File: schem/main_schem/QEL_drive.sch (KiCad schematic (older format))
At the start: 7 parts

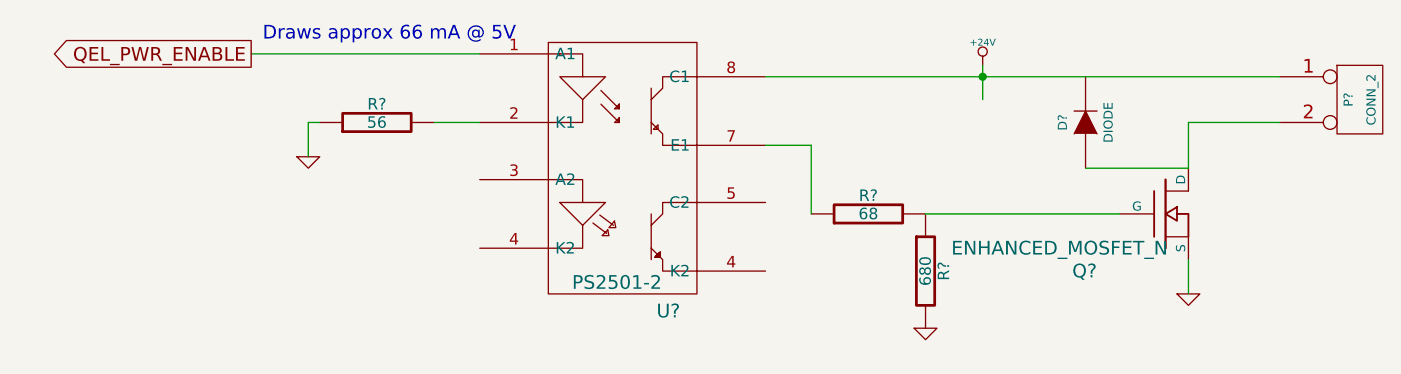
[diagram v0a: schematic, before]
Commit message: Vdd and ethernet conns to mcu
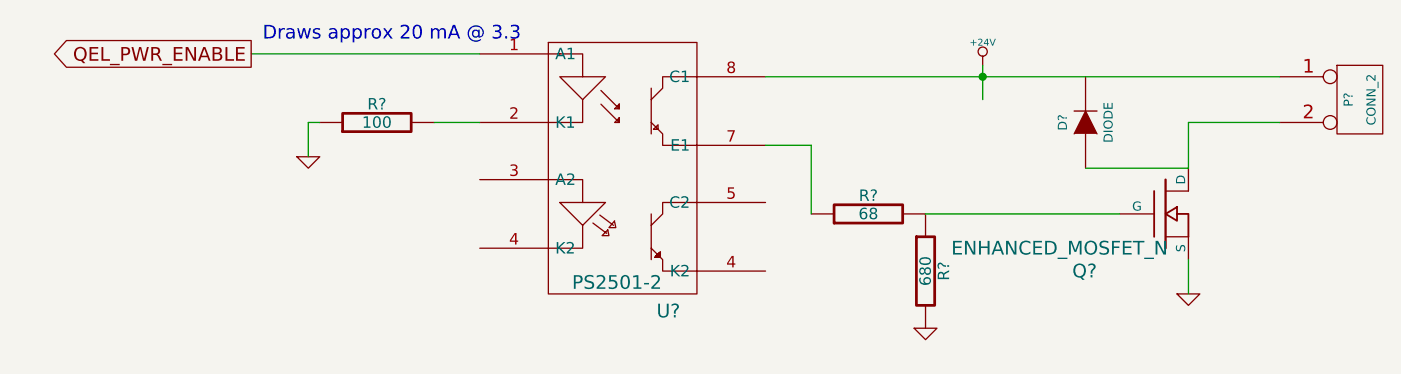
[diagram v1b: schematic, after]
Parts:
- R?: value 56 -> 100
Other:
- note added: "Draws approx 20 mA @ 3.3"
- note removed: "Draws approx 66 mA @ 5V"
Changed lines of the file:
@@
-EESchema Schematic File Version 2  date 9/18/2012 3:41:36 PM
+EESchema Schematic File Version 2  date 9/28/2012 9:39:08 AM
 LIBS:power
 LIBS:device
@@
 LIBS:valves
 LIBS:QEL
+LIBS:pic18f97j60
+LIBS:pwr
 LIBS:main_schem-cache
 EELAYER 25  0
@@
 Sheet 2 6
 Title "QEL_Driver"
-Date "18 sep 2012"
+Date "28 sep 2012"
 Rev "2"
 Comp "ECE 402 Senior Design"
@@
 $EndComp
 Text Notes 4100 3300 0    60   ~ 0
-Draws approx 66 mA @ 5V
+Draws approx 20 mA @ 3.3
 $Comp
 L R R?
@@
 P 4600 3650
 F 0 "R?" V 4680 3650 50  0000 C CNN
-F 1 "56" V 4600 3650 50  0000 C CNN
+F 1 "100" V 4600 3650 50  0000 C CNN
 	1    4600 3650
 	0    -1   -1   0

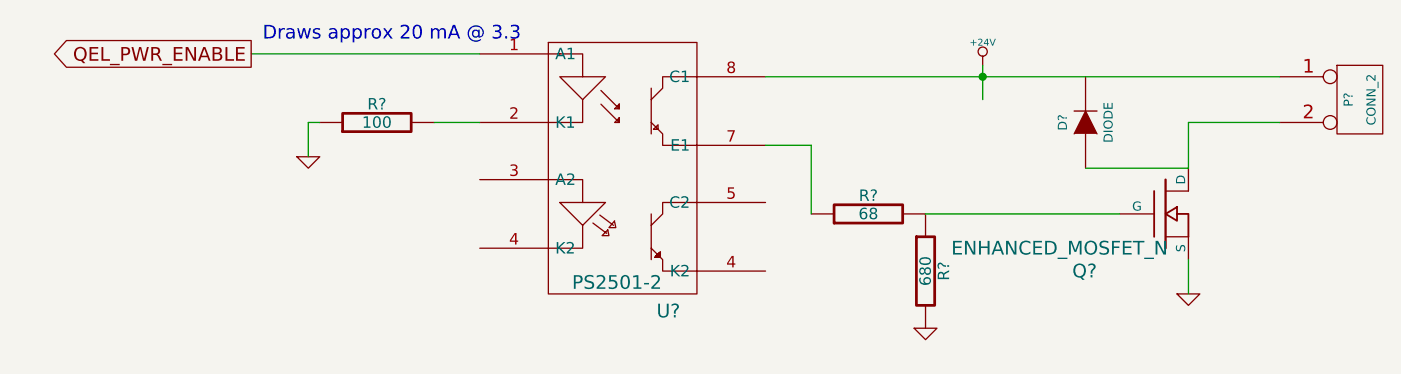
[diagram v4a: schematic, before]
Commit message: linear regulators for logic/mcu
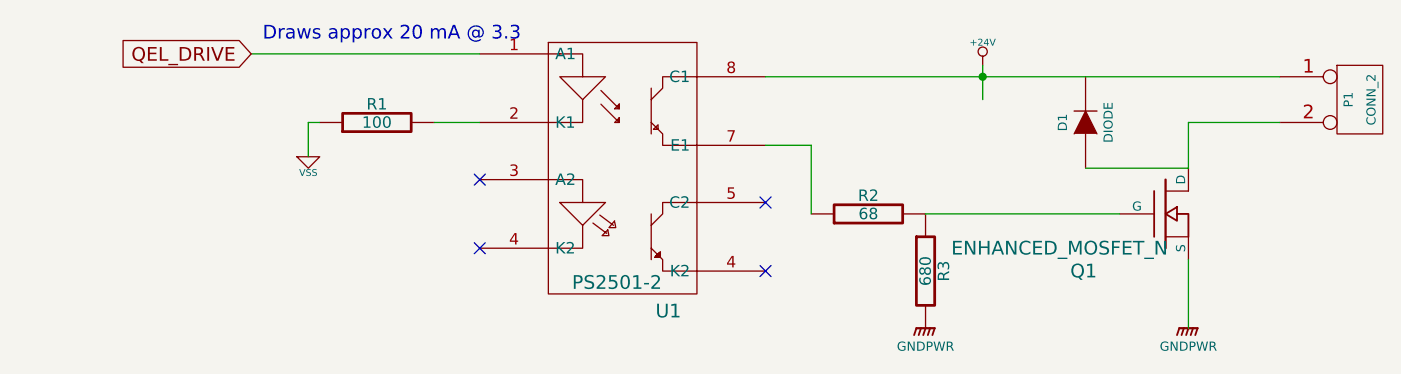
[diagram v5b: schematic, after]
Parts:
- gave numbers to parts that had none: 7
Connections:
- net labels added: GNDPWR, QEL_DRIVE, VSS
- net labels removed: GND, QEL_PWR_ENABLE
- no-connect marks 0 -> 4
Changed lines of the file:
@@
-EESchema Schematic File Version 2  date 9/29/2012 1:33:09 PM
+EESchema Schematic File Version 2  date 9/29/2012 2:30:36 PM
 LIBS:power
 LIBS:device
@@
 Comment4 ""
 $EndDescr
+Wire Wire Line
+	8150 4550 8150 4250
+Wire Wire Line
+	7000 4050 7850 4050
+Wire Wire Line
+	8150 3650 8150 3850
+Wire Wire Line
+	8550 3450 6300 3450
+Wire Wire Line
+	7250 3550 7250 3400
+Wire Wire Line
+	4850 3650 5050 3650
+Wire Wire Line
+	4050 3350 5050 3350
+Wire Wire Line
+	4350 3650 4300 3650
+Wire Wire Line
+	4300 3650 4300 3800
+Wire Wire Line
+	8150 3650 8550 3650
+Connection ~ 7250 3450
+Wire Wire Line
+	8150 3850 7700 3850
+Wire Wire Line
+	6300 3750 6500 3750
+Wire Wire Line
+	6500 3750 6500 4050
 $Comp
-L GND #PWR?
-U 1 1 5058DB93
+L GNDPWR #PWR?
+U 1 1 506747B4
+P 8150 4550
+F 0 "#PWR?" H 8150 4600 40  0001 C CNN
+F 1 "GNDPWR" H 8150 4470 40  0000 C CNN
+	1    8150 4550
+	1    0    0    -1
+$EndComp
+$Comp
+L GNDPWR #PWR?
+U 1 1 506747A8
 P 7000 4550
-F 0 "#PWR?" H 7000 4550 30  0001 C CNN
-F 1 "GND" H 7000 4480 30  0001 C CNN
+F 0 "#PWR?" H 7000 4600 40  0001 C CNN
+F 1 "GNDPWR" H 7000 4470 40  0000 C CNN
 	1    7000 4550
 	1    0    0    -1
 $EndComp
-Wire Wire Line
-	6500 3750 6500 4050
-Wire Wire Line
-	6300 3750 6500 3750
-Wire Wire Line
-	7700 3850 8150 3850
-Connection ~ 7250 3450
-Wire Wire Line
-	8550 3650 8150 3650
-Wire Wire Line
-	8150 4250 8150 4400
-Wire Wire Line
-	4300 3800 4300 3650
-Wire Wire Line
-	4300 3650 4350 3650
-Wire Wire Line
-	4050 3350 5050 3350
-Wire Wire Line
-	4850 3650 5050 3650
-Wire Wire Line
-	7250 3550 7250 3400
-Wire Wire Line
-	8550 3450 6300 3450
-Wire Wire Line
-	8150 3650 8150 3850
-Wire Wire Line
-	7000 4050 7850 4050
+NoConn ~ 6300 4300
+NoConn ~ 6300 4000
+NoConn ~ 5050 4200
+NoConn ~ 5050 3900
 $Comp
-L R R?
+L VSS #PWR1
+U 1 1 50674779
+P 4300 3800
+F 0 "#PWR1" H 4300 3800 30  0001 C CNN
+F 1 "VSS" H 4300 3730 30  0000 C CNN
+	1    4300 3800
+	1    0    0    -1
+$EndComp
+$Comp
+L R R2
 U 1 1 5058DB7E
 P 6750 4050
-F 0 "R?" V 6830 4050 50  0000 C CNN
+F 0 "R2" V 6830 4050 50  0000 C CNN
 F 1 "68" V 6750 4050 50  0000 C CNN
 	1    6750 4050
@@
 $EndComp
 $Comp
-L R R?
+L R R3
 U 1 1 5058DB66
 P 7000 4300
-F 0 "R?" V 7080 4300 50  0000 C CNN
+F 0 "R3" V 7080 4300 50  0000 C CNN
 F 1 "680" V 7000 4300 50  0000 C CNN
 	1    7000 4300
@@
 $EndComp
 $Comp
-L DIODE D?
+L DIODE D1
 U 1 1 5058DB32
 P 7700 3650
-F 0 "D?" H 7700 3750 40  0000 C CNN
+F 0 "D1" H 7700 3750 40  0000 C CNN
 F 1 "DIODE" H 7700 3550 40  0000 C CNN
 	1    7700 3650
@@
 $EndComp
 $Comp
-L MOSFET_N Q?
+L MOSFET_N Q1
 U 1 1 5058DB1C
 P 8050 4050
-F 0 "Q?" H 7750 3800 60  0000 R CNN
+F 0 "Q1" H 7750 3800 60  0000 R CNN
 F 1 "ENHANCED_MOSFET_N" H 8060 3900 60  0000 R CNN
 	1    8050 4050
@@
 $EndComp
 $Comp
-L CONN_2 P?
+L CONN_2 P1
 U 1 1 504BA571
 P 8900 3550
-F 0 "P?" V 8850 3550 40  0000 C CNN
+F 0 "P1" V 8850 3550 40  0000 C CNN
 F 1 "CONN_2" V 8950 3550 40  0000 C CNN
 	1    8900 3550
@@
 $EndComp
 $Comp
-L +24V #PWR?
+L +24V #PWR3
 U 1 1 504BA51D
 P 7250 3400
-F 0 "#PWR?" H 7250 3350 20  0001 C CNN
+F 0 "#PWR3" H 7250 3350 20  0001 C CNN
 F 1 "+24V" H 7250 3500 30  0000 C CNN
 	1    7250 3400
-	1    0    0    -1
-$EndComp
-$Comp
-L GND #PWR?
-U 1 1 504BA4EF
-P 8150 4400
-F 0 "#PWR?" H 8150 4400 30  0001 C CNN
-F 1 "GND" H 8150 4330 30  0001 C CNN
-	1    8150 4400
-	1    0    0    -1
-$EndComp
-$Comp
-L GND #PWR?
-U 1 1 504BA3D2
-P 4300 3800
-F 0 "#PWR?" H 4300 3800 30  0001 C CNN
-F 1 "GND" H 4300 3730 30  0001 C CNN
-	1    4300 3800
 	1    0    0    -1
 $EndComp
@@
 Draws approx 20 mA @ 3.3
 $Comp
-L R R?
+L R R1
 U 1 1 504B9FF4
 P 4600 3650
-F 0 "R?" V 4680 3650 50  0000 C CNN
+F 0 "R1" V 4680 3650 50  0000 C CNN
 F 1 "100" V 4600 3650 50  0000 C CNN
 	1    4600 3650
 	0    -1   -1   0
 $EndComp
-Text GLabel 4050 3350 0    60   Output ~ 0
-QEL_PWR_ENABLE
+Text GLabel 4050 3350 0    60   Input ~ 0
+QEL_DRIVE
 $Comp
-L PS2501-2 U?
+L PS2501-2 U1
 U 1 1 504B9FB2
 P 5700 3550
-F 0 "U?" H 5875 2625 60  0000 C CNN
+F 0 "U1" H 5875 2625 60  0000 C CNN
 F 1 "PS2501-2" H 5650 2750 60  0000 C CNN
 	1    5700 3550
